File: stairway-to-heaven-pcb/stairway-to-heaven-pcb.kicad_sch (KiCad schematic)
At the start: 6 parts, among them J15 PJ-063AH, U1 MEGA_PRO_EMBED_CH340G_{slash}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

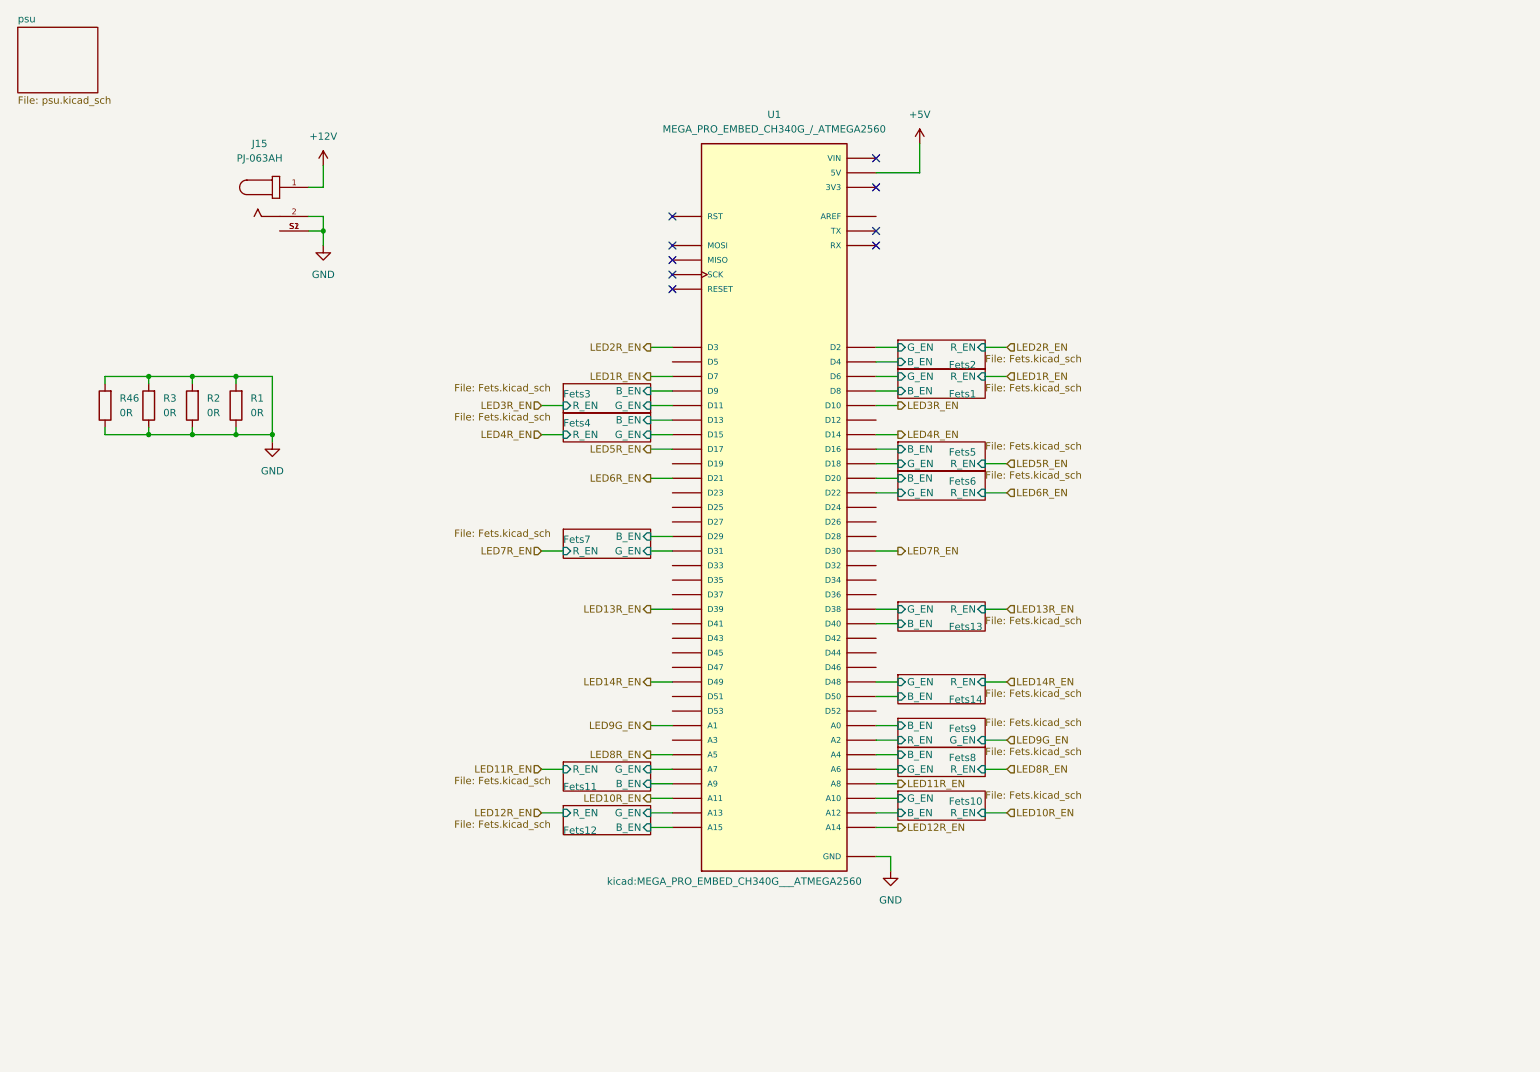
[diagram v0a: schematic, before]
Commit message: Change to 4 layer pcb. Routing leds done.
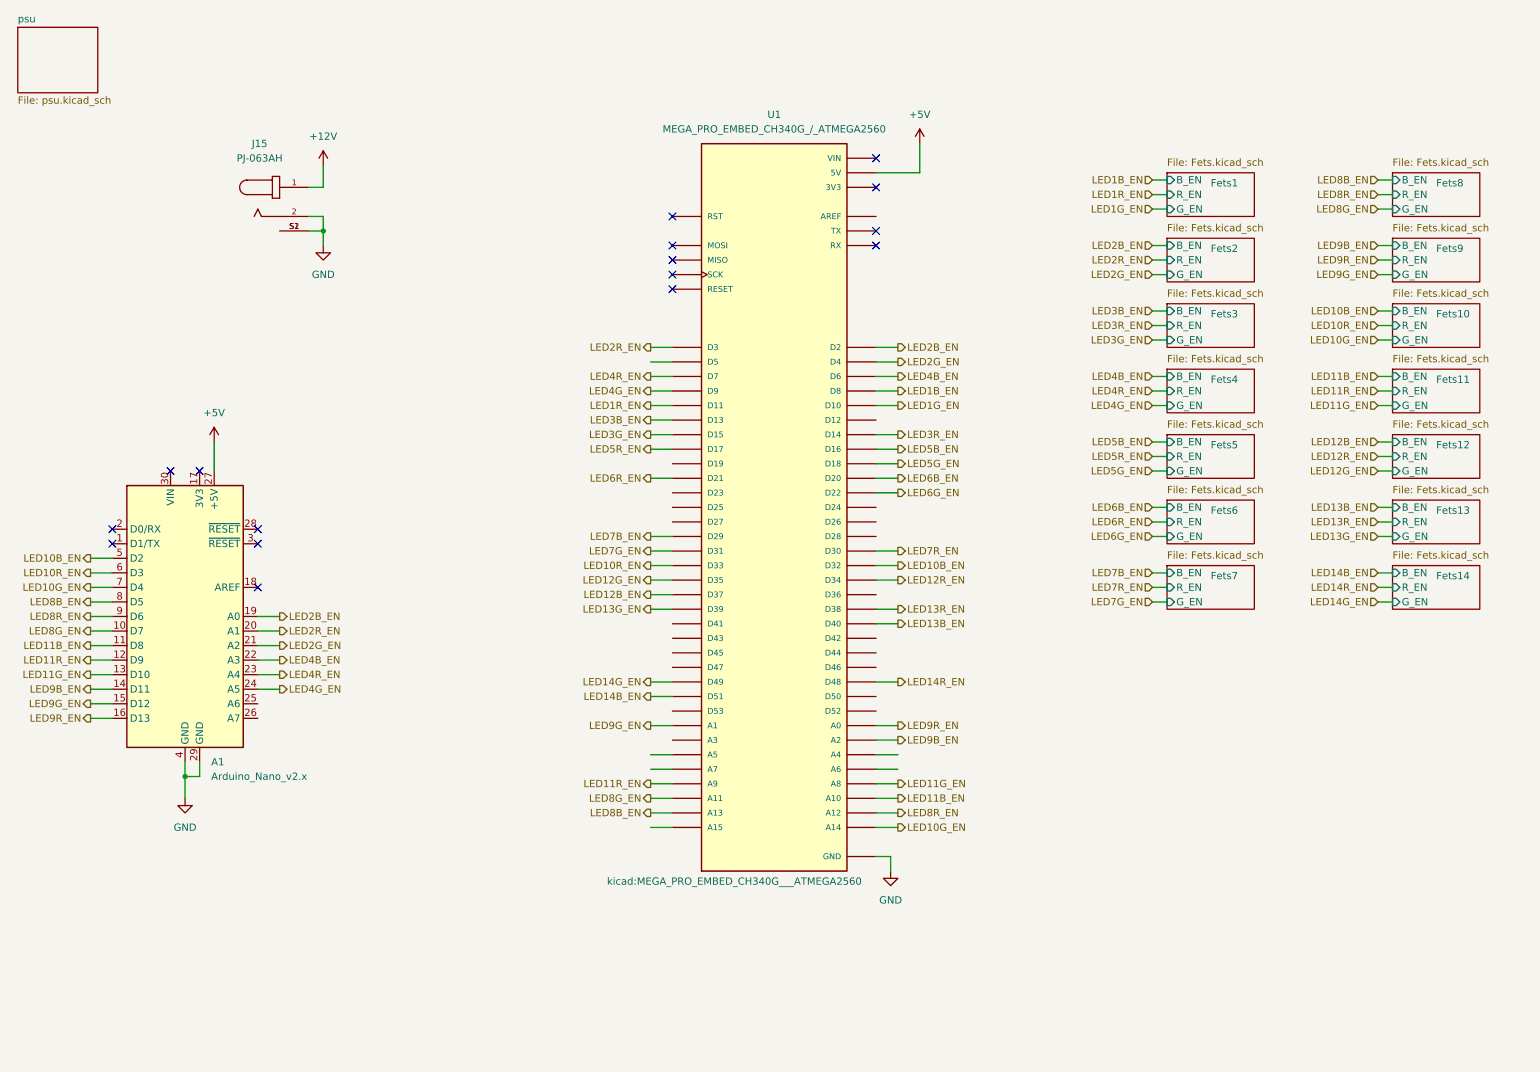
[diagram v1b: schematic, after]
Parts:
- removed R1, R2, R3, R46: 0R, Resistor_SMD:R_1206_3216Metric, symbol Device:R
- added A1: Arduino_Nano_v2.x, Module:Arduino_Nano, symbol MCU_Module:Arduino_Nano_v2.x
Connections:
- net Fets10/B_EN is gone; now on net LED8R_EN: U1.A12
- net Fets11/B_EN is gone; now on net LED11R_EN: U1.A9
- net Fets13/G_EN is gone; now on net LED13R_EN: U1.D38
- net Fets14/G_EN is gone; now on net LED14R_EN: U1.D48
- net Fets3/G_EN is gone; now on net LED1R_EN: U1.D11
- net +5V: now also A1.27 (+5V)
- net GND: now also A1.29 (GND), A1.4 (GND)
- net LED10R_EN: now also U1.D33, A1.6 (D3); no longer U1.A11
- net LED11R_EN: now also A1.12 (D9); no longer U1.A8
- net LED12R_EN: now also U1.D34; no longer U1.A14
- net LED13R_EN: no longer U1.D39
- net LED14R_EN: no longer U1.D49
- net LED1R_EN: no longer U1.D7
- net LED2R_EN: now also A1.20 (A1)
- net LED3R_EN: now also U1.D14; no longer U1.D10
- net LED4R_EN: now also U1.D7, A1.23 (A4); no longer U1.D14
- net LED8R_EN: now also A1.9 (D6); no longer U1.A5
- net LED9G_EN: now also A1.15 (D12)
- net LED10B_EN: now reaches U1.D32
- net LED10B_EN: now also A1.5 (D2)
- net LED12G_EN: now reaches U1.D35
- net LED12B_EN: now reaches U1.D37
- net LED14B_EN: now reaches U1.D51
- net Fets1/B_EN renamed LED1B_EN
- net Fets1/G_EN renamed LED4B_EN
- net LED4B_EN: now also A1.22 (A3)
- net Fets10/G_EN renamed LED11B_EN
- net LED11B_EN: now also A1.11 (D8)
- net Fets11/G_EN: no longer names the net of U1.A7
- net Fets12/B_EN: no longer names the net of U1.A15
- net Fets12/G_EN renamed LED8B_EN
- net LED8B_EN: now also A1.8 (D5)
- net Fets13/B_EN renamed LED13B_EN
- net Fets14/B_EN: no longer names the net of U1.D50
- net Fets2/B_EN renamed LED2G_EN
- net LED2G_EN: now also A1.21 (A2)
- net Fets2/G_EN renamed LED2B_EN
- net LED2B_EN: now also A1.19 (A0)
- net Fets3/B_EN renamed LED4G_EN
- net LED4G_EN: now also A1.24 (A5)
- net Fets4/B_EN renamed LED3B_EN
- net Fets4/G_EN renamed LED3G_EN
- net Fets5/B_EN renamed LED5B_EN
- net Fets5/G_EN renamed LED5G_EN
- net Fets6/B_EN renamed LED6B_EN
- net Fets6/G_EN renamed LED6G_EN
- net Fets7/B_EN renamed LED7B_EN
- net Fets7/G_EN renamed LED7G_EN
- net Fets8/B_EN: no longer names the net of U1.A4
- net Fets8/G_EN: no longer names the net of U1.A6
- net Fets9/B_EN renamed LED9R_EN
- net LED9R_EN: now also A1.16 (D13)
- net Fets9/R_EN renamed LED9B_EN
- net LED9B_EN: now also A1.14 (D11)
- new net LED10G_EN: A1.7 (D4), U1.A14
- new net LED11G_EN: A1.13 (D10), U1.A8
- new net LED13G_EN: U1.D39
- new net LED14G_EN: U1.D49
- new net LED1G_EN: U1.D10
- new net LED8G_EN: A1.10 (D7), U1.A11
- no-connect marks 9 -> 16

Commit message: PSU, again.. Stitching. Moved arduino nano.
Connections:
- net LED11B_EN: now also U1.A7; no longer U1.A10
- net LED11G_EN: now also U1.A4; no longer U1.A8
- net LED11R_EN: now also U1.A5; no longer U1.A9
- net LED8G_EN: now also U1.A9; no longer U1.A11
- net LED8R_EN: now also U1.A11; no longer U1.A12
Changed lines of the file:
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@@
     (effects (font (size 1.27 1.27)) (justify right))
   )
-  (hierarchical_label "LED11G_EN" (shape output) (at 168.91 148.59 0)
+  (hierarchical_label "LED11G_EN" (shape output) (at 168.91 143.51 0)
     (effects (font (size 1.27 1.27)) (justify left))
   )
@@
     (effects (font (size 1.27 1.27)) (justify left))
   )
-  (hierarchical_label "LED11R_EN" (shape output) (at 125.73 148.59 180)
+  (hierarchical_label "LED11R_EN" (shape output) (at 125.73 143.51 180)
     (effects (font (size 1.27 1.27)) (justify right))
   )
@@
     (effects (font (size 1.27 1.27)) (justify left))
   )
-  (hierarchical_label "LED8G_EN" (shape output) (at 125.73 151.13 180)
+  (hierarchical_label "LED8G_EN" (shape output) (at 125.73 148.59 180)
     (effects (font (size 1.27 1.27)) (justify right))
   )
@@
     (effects (font (size 1.27 1.27)) (justify left))
   )
-  (hierarchical_label "LED11B_EN" (shape output) (at 168.91 151.13 0)
-    (effects (font (size 1.27 1.27)) (justify left))
+  (hierarchical_label "LED11B_EN" (shape output) (at 125.73 146.05 180)
+    (effects (font (size 1.27 1.27)) (justify right))
   )
   (hierarchical_label "LED11R_EN" (shape input) (at 252.73 80.01 180)
@@
     (effects (font (size 1.27 1.27)) (justify right))
   )
-  (hierarchical_label "LED8R_EN" (shape output) (at 168.91 153.67 0)
-    (effects (font (size 1.27 1.27)) (justify left))
+  (hierarchical_label "LED8R_EN" (shape output) (at 125.73 151.13 180)
+    (effects (font (size 1.27 1.27)) (justify right))
   )
   (hierarchical_label "LED7R_EN" (shape input) (at 213.36 114.3 180)

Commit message: Add CA6V potentiometer footprint. Mounting holes.
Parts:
- added H1, H2, H3: MountingHole_Pad, MountingHole:MountingHole_2.2mm_M2_DIN965_Pad, symbol Mechanical:MountingHole_Pad
- added RV100k1: R_Potentiometer_Trim, CA6V Potentiometer THT:CA6V-NoMidHole, symbol Device:R_Potentiometer_Trim
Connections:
- net +5V: now also RV100k1.1
- net GND: now also H1.1, H2.1, H3.1, RV100k1.3
- net POT1: now reaches U1.A15
- net POT1: now also RV100k1.2
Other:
- moved on the sheet: J15

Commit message: Silks, small mods
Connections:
- no-connect marks 16 -> 39
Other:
- title: (none) -> Stairway to Heaven
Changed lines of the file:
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@@
 (kicad_sch (version 20211123) (generator eeschema)
   (paper "A4")
+  (title_block
+    (title "Stairway to Heaven")
+  )
   (junction (at 52.07 52.07) (diameter 0) (color 0 0 0 0)
   )
@@
   (junction (at 44.45 147.32) (diameter 0) (color 0 0 0 0)
   )
+  (no_connect (at 57.15 137.16))
+  (no_connect (at 57.15 134.62))
+  (no_connect (at 129.54 102.87))
+  (no_connect (at 129.54 100.33))
+  (no_connect (at 129.54 97.79))
+  (no_connect (at 129.54 74.93))
+  (no_connect (at 129.54 92.71))
+  (no_connect (at 165.1 135.89))
+  (no_connect (at 165.1 133.35))
+  (no_connect (at 165.1 123.19))
+  (no_connect (at 165.1 128.27))
+  (no_connect (at 165.1 125.73))
+  (no_connect (at 129.54 135.89))
+  (no_connect (at 129.54 128.27))
+  (no_connect (at 129.54 123.19))
+  (no_connect (at 129.54 125.73))
+  (no_connect (at 129.54 120.65))
+  (no_connect (at 165.1 49.53))
+  (no_connect (at 165.1 85.09))
+  (no_connect (at 165.1 100.33))
+  (no_connect (at 165.1 102.87))
+  (no_connect (at 165.1 105.41))
+  (no_connect (at 165.1 115.57))
   (no_connect (at 41.91 93.98))
   (no_connect (at 46.99 93.98))
@@
     (stroke (width 0) (type default) (color 0 0 0 0))
   )
-  (wire (pts (xy 165.1 153.67) (xy 168.91 153.67))
-    (stroke (width 0) (type default) (color 0 0 0 0))
-  )
   (wire (pts (xy 125.73 72.39) (xy 129.54 72.39))
     (stroke (width 0) (type default) (color 0 0 0 0))
@@
     (stroke (width 0) (type default) (color 0 0 0 0))
   )
-  (wire (pts (xy 165.1 151.13) (xy 168.91 151.13))
-    (stroke (width 0) (type default) (color 0 0 0 0))
-  )
   (wire (pts (xy 213.36 77.47) (xy 215.9 77.47))
     (stroke (width 0) (type default) (color 0 0 0 0))
@@
     (stroke (width 0) (type default) (color 0 0 0 0))
   )
-  (wire (pts (xy 125.73 74.93) (xy 129.54 74.93))
-    (stroke (width 0) (type default) (color 0 0 0 0))
-  )
   (wire (pts (xy 213.36 111.76) (xy 215.9 111.76))
     (stroke (width 0) (type default) (color 0 0 0 0))
@@
     (stroke (width 0) (type default) (color 0 0 0 0))
   )
-  (wire (pts (xy 165.1 146.05) (xy 168.91 146.05))
-    (stroke (width 0) (type default) (color 0 0 0 0))
-  )
   (wire (pts (xy 213.36 93.98) (xy 215.9 93.98))
     (stroke (width 0) (type default) (color 0 0 0 0))
@@
     (stroke (width 0) (type default) (color 0 0 0 0))
   )
-  (wire (pts (xy 165.1 148.59) (xy 168.91 148.59))
-    (stroke (width 0) (type default) (color 0 0 0 0))
-  )

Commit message: Add sensor drawing
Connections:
- net SENSOR1: now reaches U1.D44
- no-connect marks 39 -> 38
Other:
- added sheet Sensor (Sensor.kicad_sch)
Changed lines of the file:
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@@
   (no_connect (at 165.1 123.19))
   (no_connect (at 165.1 128.27))
-  (no_connect (at 165.1 125.73))
   (no_connect (at 129.54 135.89))
   (no_connect (at 129.54 128.27))
@@
     (stroke (width 0) (type default) (color 0 0 0 0))
   )
+  (wire (pts (xy 213.36 132.08) (xy 215.9 132.08))
+    (stroke (width 0) (type default) (color 0 0 0 0))
+  )
   (wire (pts (xy 165.1 72.39) (xy 168.91 72.39))
     (stroke (width 0) (type default) (color 0 0 0 0))
@@
     (stroke (width 0) (type default) (color 0 0 0 0))
   )
+  (wire (pts (xy 165.1 125.73) (xy 168.91 125.73))
+    (stroke (width 0) (type default) (color 0 0 0 0))
+  )
   (wire (pts (xy 125.73 107.95) (xy 129.54 107.95))
     (stroke (width 0) (type default) (color 0 0 0 0))
@@
     (effects (font (size 1.27 1.27)) (justify right))
   )
+  (hierarchical_label "SENSOR1" (shape input) (at 168.91 125.73 0)
+    (effects (font (size 1.27 1.27)) (justify left))
+  )
   (hierarchical_label "POT1" (shape input) (at 100.33 46.99 0)
     (effects (font (size 1.27 1.27)) (justify left))
@@
   )
   (hierarchical_label "LED7B_EN" (shape output) (at 125.73 105.41 180)
+    (effects (font (size 1.27 1.27)) (justify right))
+  )
+  (hierarchical_label "SENSOR1" (shape output) (at 213.36 132.08 180)
     (effects (font (size 1.27 1.27)) (justify right))
   )
@@
     )
   )
+  (sheet (at 215.9 129.54) (size 15.24 5.08) (fields_autoplaced)
+    (stroke (width 0.1524) (type solid) (color 0 0 0 0))
+    (fill (color 0 0 0 0.0000))
+    (property "Sheet name" "Sensor" (id 0) (at 215.9 128.8284 0)
+      (effects (font (size 1.27 1.27)) (justify left bottom))
+    )
+    (property "Sheet file" "Sensor.kicad_sch" (id 1) (at 215.9 135.2046 0)
+      (effects (font (size 1.27 1.27)) (justify left top))
+    )
+    (pin "S_OUT" output (at 215.9 132.08 180)
+      (effects (font (size 1.27 1.27)) (justify left))
+    )
+  )
   (sheet (at 215.9 87.63) (size 15.24 7.62)
     (stroke (width 0.1524) (type solid) (color 0 0 0 0))
@@
     (path "/e669b97c-3437-4faa-b176-8136fb97a507" (page "15"))
     (path "/c11913c3-97db-4bc4-9b11-925f21417dd2" (page "16"))
+    (path "/e0460e84-fae2-4f7a-9cb4-b83428d4856d" (page "17"))
   )
   (symbol_instances
@@
       (reference "#PWR0183") (unit 1) (value "GND") (footprint "")
     )
+    (path "/e0460e84-fae2-4f7a-9cb4-b83428d4856d/48bef4dd-ed57-41aa-8bfb-d20dd2f1a8f2"
+      (reference "#PWR?") (unit 1) (value "GND") (footprint "")
+    )
+    (path "/e0460e84-fae2-4f7a-9cb4-b83428d4856d/7cdebfb6-ee5d-4f3c-93f2-162bb3ad0c00"
+      (reference "#PWR?") (unit 1) (value "+5V") (footprint "")
+    )
     (path "/66749c6a-b16f-43be-bab1-76caa7a8a44a"
       (reference "A1") (unit 1) (value "Arduino_Nano_v2.x") (footprint "Module:Arduino_Nano")
@@
       (reference "J15") (unit 1) (value "PJ-063AH") (footprint "kicad-ss-libs:CUI_PJ-063AH")
     )
+    (path "/e0460e84-fae2-4f7a-9cb4-b83428d4856d/b30beb01-612e-4638-8ee9-9492c30366f2"
+      (reference "J?") (unit 1) (value "Conn_01x03_Male") (footprint "Connector_PinHeader_2.54mm:PinHeader_1x03_P2.54mm_Vertical")
+    )
     (path "/c11913c3-97db-4bc4-9b11-925f21417dd2/975b62c4-8cdb-45c2-8dea-3070ff20cf21"
       (reference "L1") (unit 1) (value "100uH") (footprint "Inductor_SMD:L_10.4x10.4_H4.8")
@@
       (reference "R45") (unit 1) (value "50k") (footprint "Resistor_SMD:R_0805_2012Metric")
     )
+    (path "/e0460e84-fae2-4f7a-9cb4-b83428d4856d/483a6339-023f-4380-b088-f4c15b1dfb16"
+      (reference "R?") (unit 1) (value "100k") (footprint "Resistor_SMD:R_0805_2012Metric")
+    )
     (path "/e5625f2f-35b3-4300-8687-f8ee31e46cf1"

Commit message: Add terminal for sensors
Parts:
- added J16: Conn_01x06_Male, ScrewTerminal-5_08:ScrewTerminal-5_08-6, symbol Connector:Conn_01x06_Male
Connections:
- net +5V: now also J16.3 (Pin_3)
- net GND: now also J16.4 (Pin_4)
- net LED7B_EN: now also U1.D26; no longer U1.D29
- net LED7R_EN: now also U1.D29; no longer U1.D30
- net SENSOR1: now also U1.D52, J16.1 (Pin_1); no longer U1.D44
- net SENSOR4: now reaches U1.D28
- net SENSOR4: now also A1.25 (A6), J16.6 (Pin_6)
- net SENSOR2: now reaches U1.D53
- net SENSOR2: now also J16.2 (Pin_2)
- net SENSOR3: now reaches A1.26 (A7)
- net SENSOR3: now also U1.D30, J16.5 (Pin_5)
- no-connect marks 38 -> 32
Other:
- removed sheet Sensor

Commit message: Final touches
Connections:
- no-connect marks 32 -> 38
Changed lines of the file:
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@@
   (no_connect (at 31.75 106.68))
   (no_connect (at 31.75 104.14))
+  (no_connect (at 165.1 125.73))
+  (no_connect (at 165.1 146.05))
+  (no_connect (at 165.1 148.59))
+  (no_connect (at 165.1 151.13))
+  (no_connect (at 129.54 140.97))
+  (no_connect (at 165.1 153.67))
   (no_connect (at 165.1 39.37))
   (wire (pts (xy 27.94 109.22) (xy 31.75 109.22))
@@
     (stroke (width 0) (type default) (color 0 0 0 0))
   )
-  (wire (pts (xy 165.1 125.73) (xy 168.91 125.73))
-    (stroke (width 0) (type default) (color 0 0 0 0))
-  )
